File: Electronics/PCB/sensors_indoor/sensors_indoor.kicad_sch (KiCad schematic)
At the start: 15 parts, among them J1 USB4125-GF-A, U1 MIC5219-3.3YM5

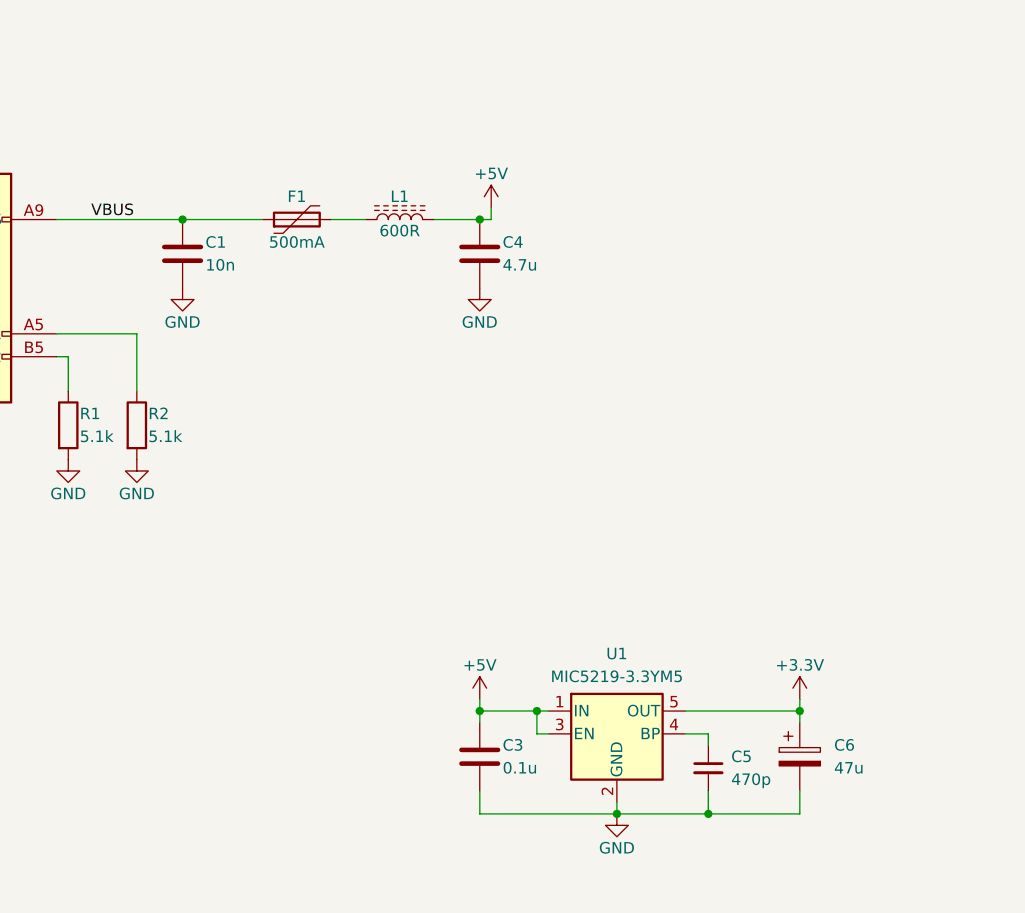
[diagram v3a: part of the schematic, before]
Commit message: Swapped sides of everything and started routing
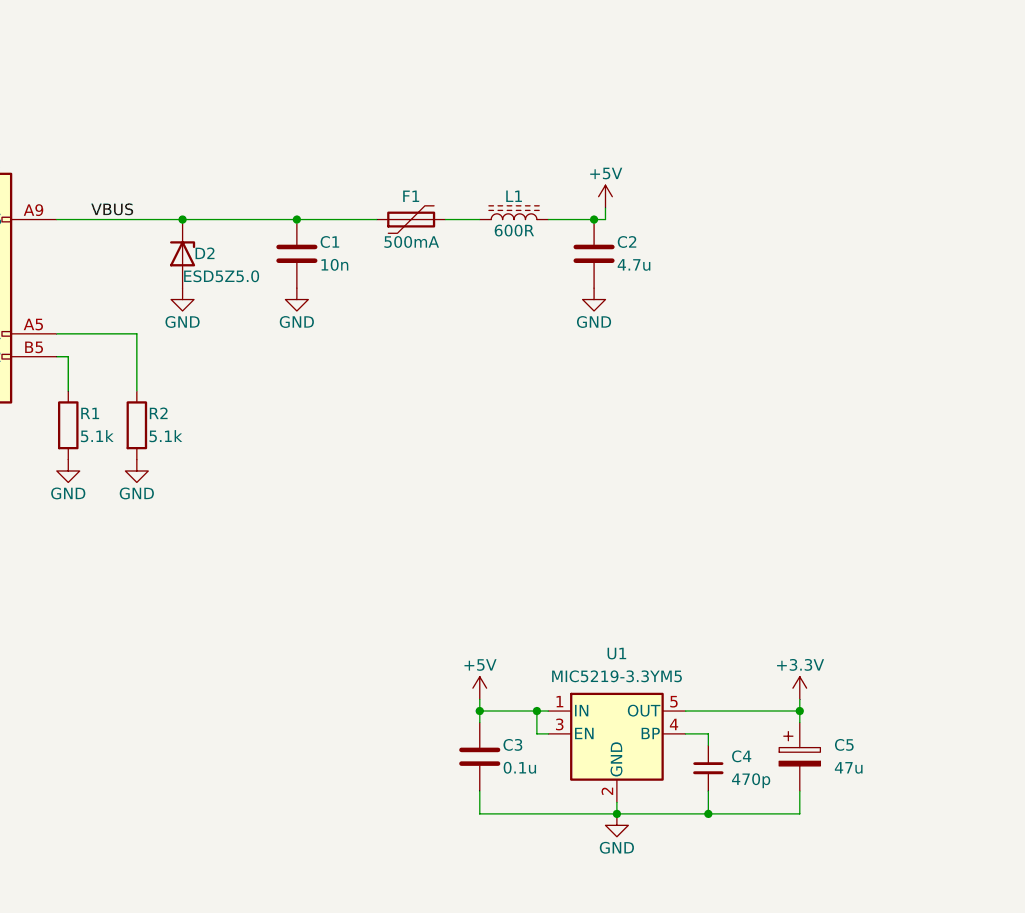
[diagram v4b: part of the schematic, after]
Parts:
- added D2: ESD5Z5.0, Diode_SMD:D_SOD-523, symbol Diode:ESD5Zxx
- C1: footprint (none) -> Capacitor_SMD:C_0402_1005Metric
- C4: renamed from C5; footprint (none) -> Capacitor_SMD:C_0402_1005Metric
- renumbered C4 to C2, C6 to C5
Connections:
- net GND: now also D2.2 (A)
- net VBUS: now also D2.1 (K)
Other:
- moved on the sheet: C1, C2, F1, L1

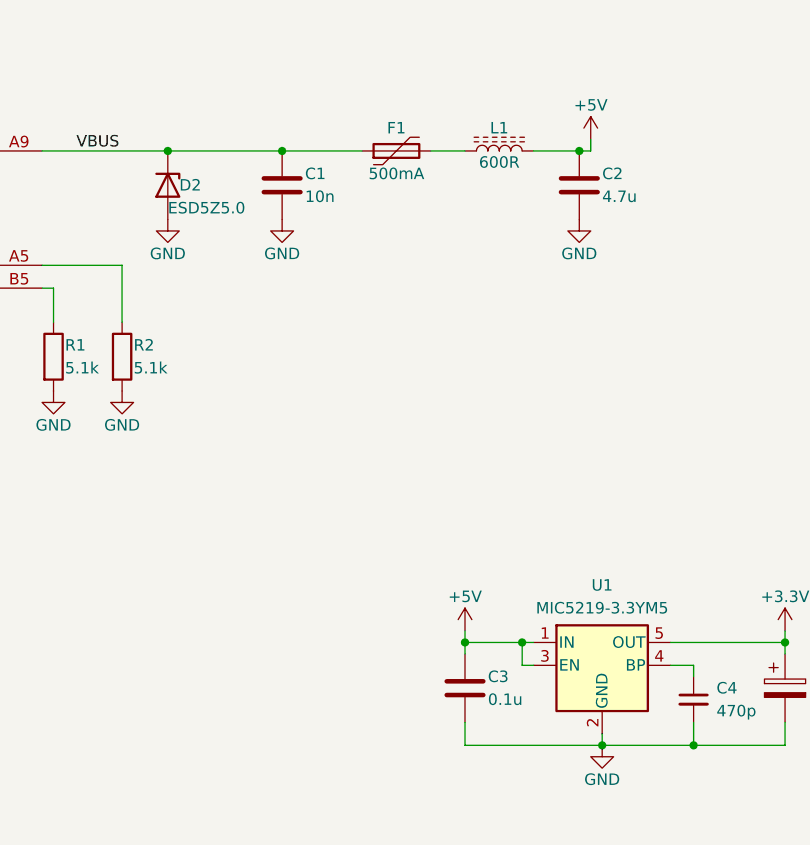
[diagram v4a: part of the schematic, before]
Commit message: Completed schematic, done most routing
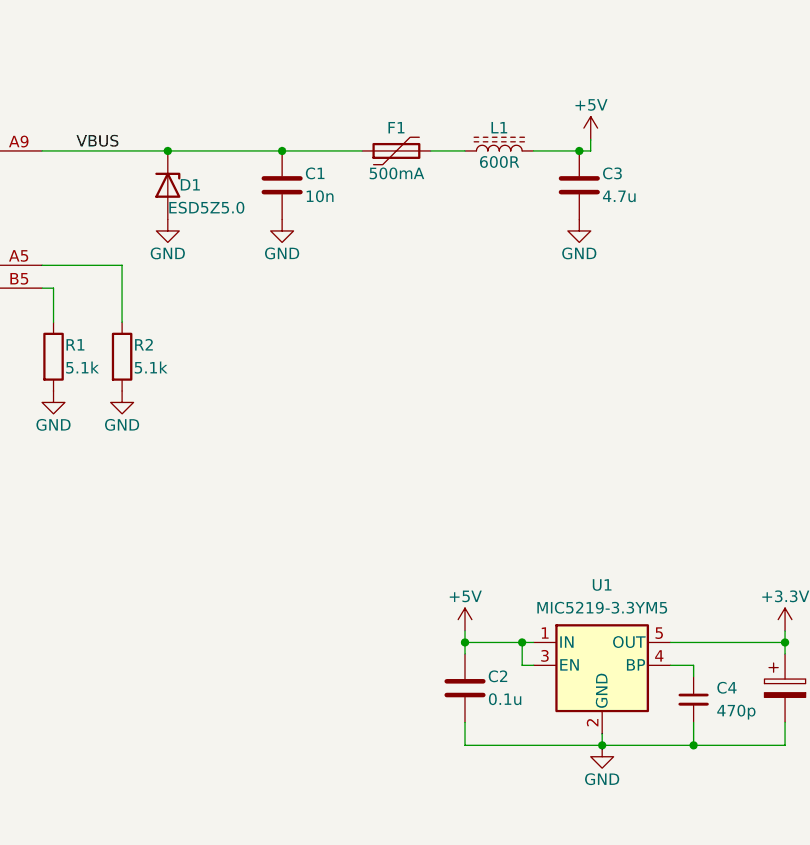
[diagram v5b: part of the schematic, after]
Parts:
- renumbered C3 to C2, C2 to C3, D2 to D1
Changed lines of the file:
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@@
 		(on_board yes)
 		(dnp no)
-		(property "Reference" "C3"
+		(property "Reference" "C2"
 			(at 106.68 100.33 0)
 			(effects
@@
 			(project "sensors_indoor"
 				(path "/09bb465b-75b9-463f-b128-e813d3269ff6"
-					(reference "C3")
+					(reference "C2")
 					(unit 1)
 				)
@@
 		(on_board yes)
 		(dnp no)
-		(property "Reference" "C2"
+		(property "Reference" "C3"
 			(at 119.38 44.45 0)
 			(effects
@@
 			(project "sensors_indoor"
 				(path "/09bb465b-75b9-463f-b128-e813d3269ff6"
-					(reference "C2")
+					(reference "C3")
 					(unit 1)
 				)
@@
 		(on_board yes)
 		(dnp no)
-		(property "Reference" "#PWR05"
+		(property "Reference" "#PWR06"
 			(at 83.82 55.88 0)
 			(effects
@@
 			(project "sensors_indoor"
 				(path "/09bb465b-75b9-463f-b128-e813d3269ff6"
-					(reference "#PWR05")
+					(reference "#PWR06")
 					(unit 1)
 				)
@@
 		(on_board yes)
 		(dnp no)
-		(property "Reference" "#PWR057"
+		(property "Reference" "#PWR05"
 			(at 71.12 55.88 0)
 			(effects
@@
 			(project "sensors_indoor"
 				(path "/09bb465b-75b9-463f-b128-e813d3269ff6"
-					(reference "#PWR057")
+					(reference "#PWR05")
 					(unit 1)
 				)
@@
 		(on_board yes)
 		(dnp no)
-		(property "Reference" "#PWR06"
+		(property "Reference" "#PWR08"
 			(at 116.84 55.88 0)
 			(effects
@@
 			(project "sensors_indoor"
 				(path "/09bb465b-75b9-463f-b128-e813d3269ff6"
-					(reference "#PWR06")
+					(reference "#PWR08")
 					(unit 1)
 				)
@@
 		(on_board yes)
 		(dnp no)
-		(property "Reference" "#PWR010"
+		(property "Reference" "#PWR011"
 			(at 139.7 99.06 0)
 			(effects
@@
 			(project "sensors_indoor"
 				(path "/09bb465b-75b9-463f-b128-e813d3269ff6"
-					(reference "#PWR010")
+					(reference "#PWR011")
 					(unit 1)
 				)
@@
 		(on_board yes)
 		(dnp no)
-		(property "Reference" "#PWR08"
+		(property "Reference" "#PWR09"
 			(at 118.11 44.45 0)
 			(effects
@@
 			(project "sensors_indoor"
 				(path "/09bb465b-75b9-463f-b128-e813d3269ff6"
-					(reference "#PWR08")
+					(reference "#PWR09")
 					(unit 1)
 				)
@@
 		(on_board yes)
 		(dnp no)
-		(property "Reference" "D2"
+		(property "Reference" "D1"
 			(at 72.39 45.72 90)
 			(effects
@@
 			(project ""
 				(path "/09bb465b-75b9-463f-b128-e813d3269ff6"
-					(reference "D2")
+					(reference "D1")
 					(unit 1)
 				)
@@
 		(on_board yes)
 		(dnp no)
-		(property "Reference" "#PWR09"
+		(property "Reference" "#PWR010"
 			(at 119.38 114.3 0)
 			(effects
@@
 			(project "sensors_indoor"
 				(path "/09bb465b-75b9-463f-b128-e813d3269ff6"
-					(reference "#PWR09")
-					(unit 1)
-				)
+					(reference "#PWR010")
+					(unit 1)
+				)
